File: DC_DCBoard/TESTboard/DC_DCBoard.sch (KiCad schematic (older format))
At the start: 26 parts, among them J1 TSV, J2 12V_OUT, J3 Conn_01x05, U1 DCM4623TD2J13D0T70, U2 LTV-817S, U3 TLP184, U4 LTV-817S

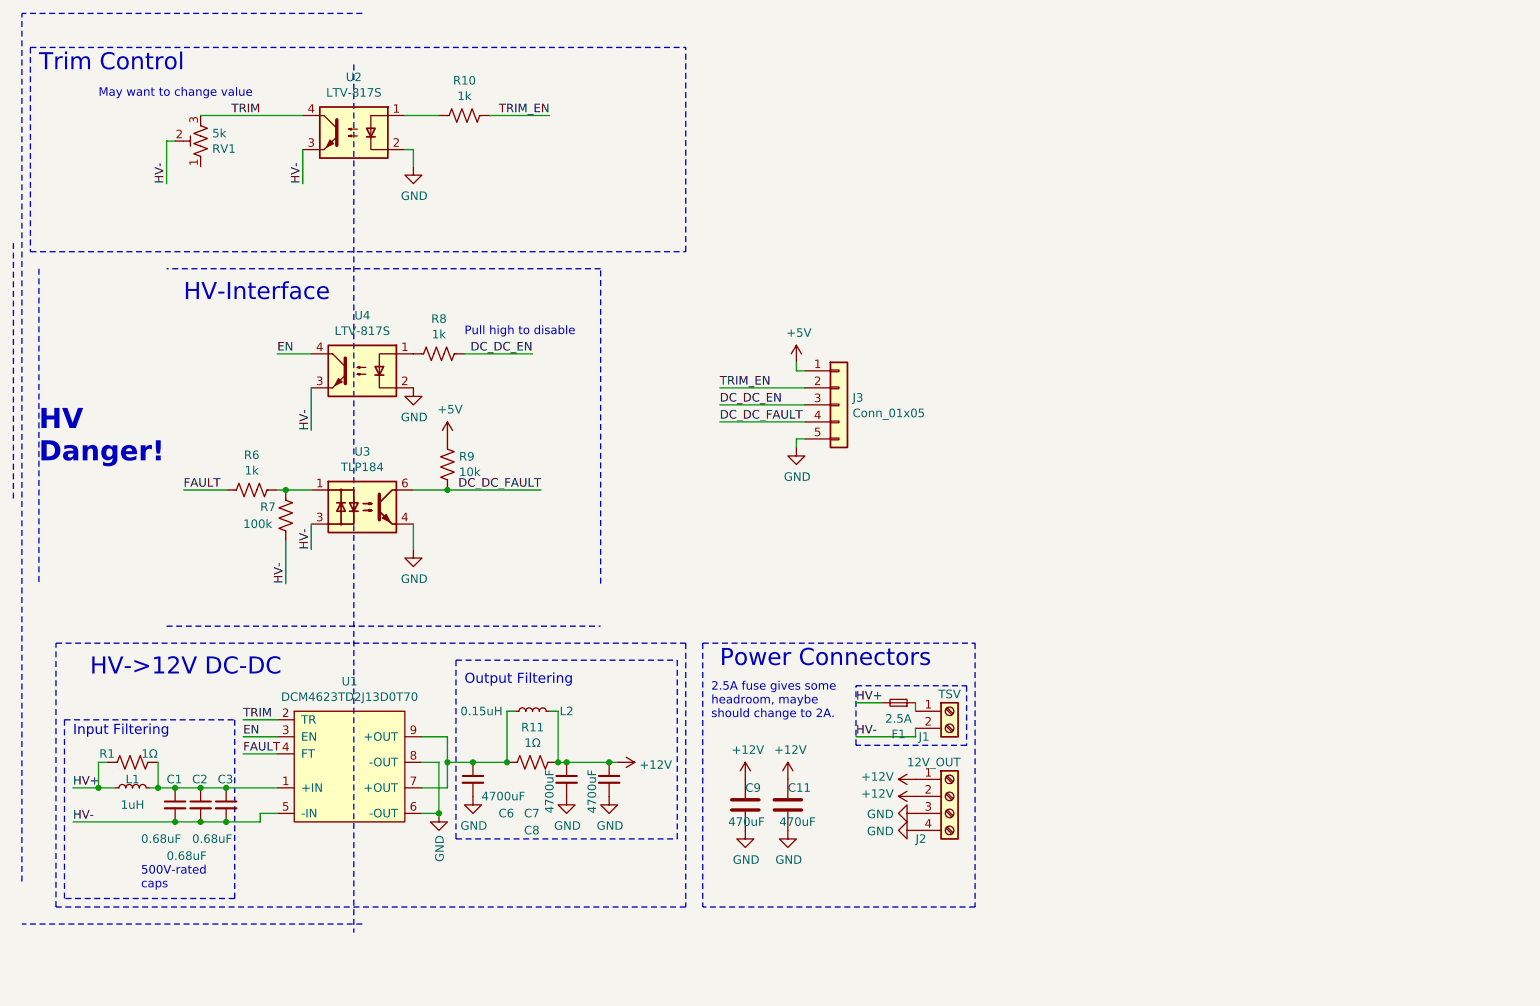
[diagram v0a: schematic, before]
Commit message: Made PDF schematic of DC/DC test board
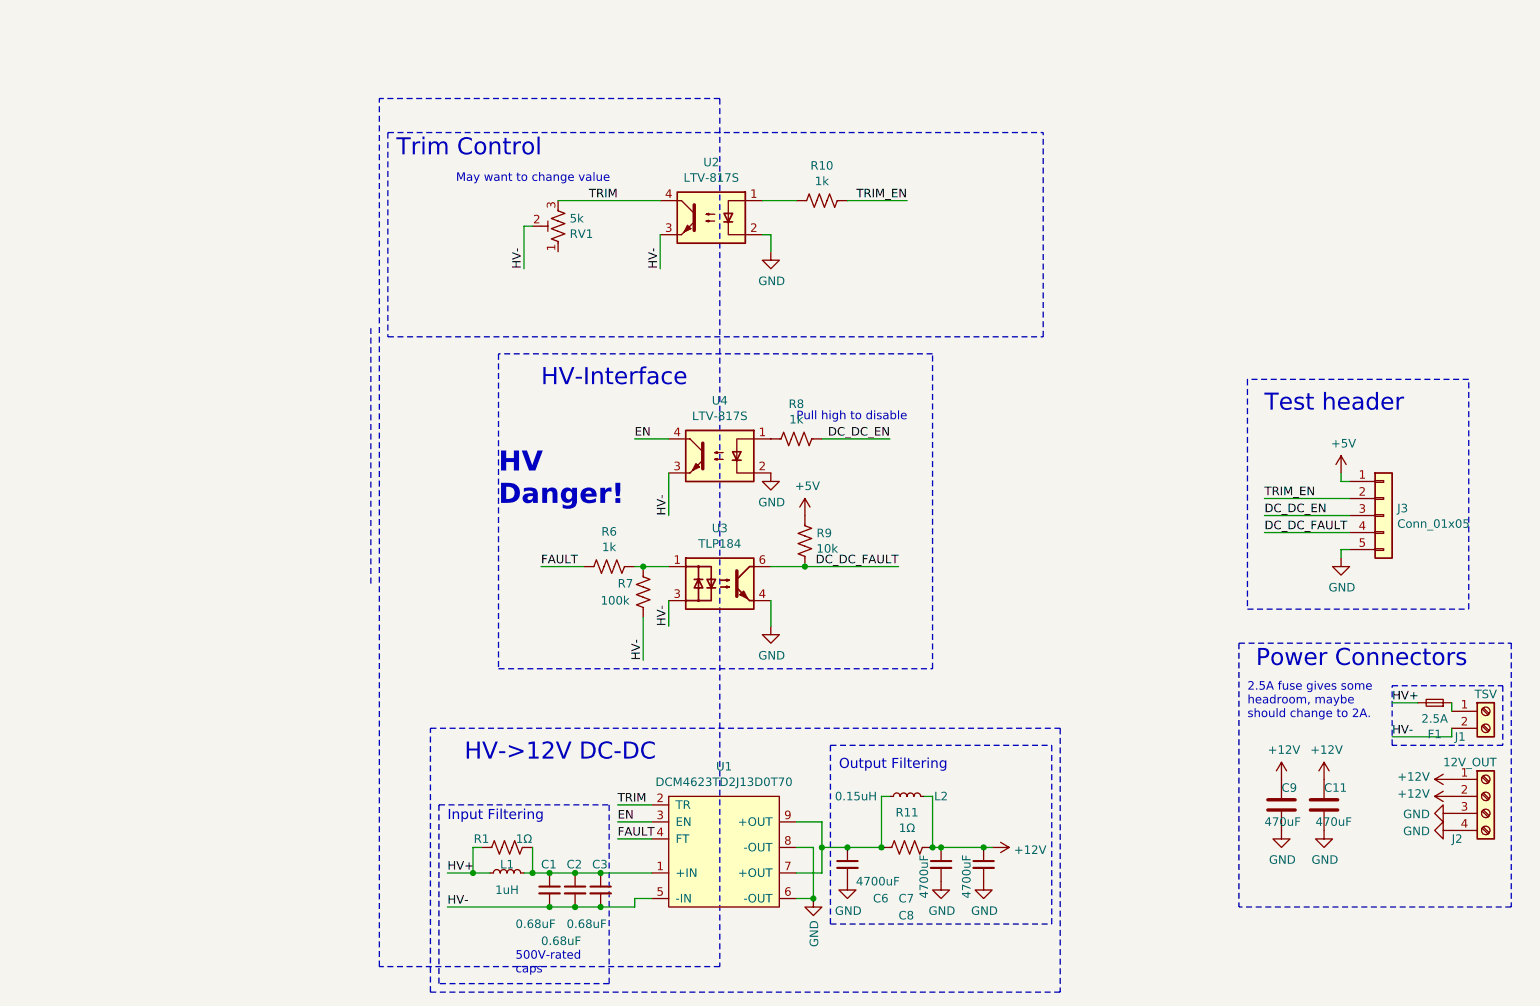
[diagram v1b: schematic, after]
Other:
- note added: "Test header"
- moved on the sheet: C1, C11, C2, C3, C6, C7, C8, C9, F1, J1, J2, J3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

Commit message: Fixed pot value on test board
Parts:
- added R2: 6.8k, Resistor_SMD:R_0603_1608Metric, symbol Device:R_US
- RV1: value 5k -> 50k; footprint Potentiometer_THT:Potentiometer_Piher_PT-15-V02_Vertical -> CustomFootprints:TC33X-503ECT-ND
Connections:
- net HV-: now also R2.2; no longer RV1.2
- new net: R2.1, RV1.2
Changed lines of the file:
@@
 P 3700 1800
 F 0 "RV1" H 3632 1846 50  0000 R CNN
-F 1 "5k" H 3632 1755 50  0000 R CNN
-F 2 "Potentiometer_THT:Potentiometer_Piher_PT-15-V02_Vertical" H 3700 1800 50  0001 C CNN
+F 1 "50k" H 3632 1755 50  0000 R CNN
+F 2 "CustomFootprints:TC33X-503ECT-ND" H 3700 1800 50  0001 C CNN
 F 3 "~" H 3700 1800 50  0001 C CNN
 	1    3700 1800
@@
 Wire Notes Line
 	2700 1250 6550 1250
-Text Label 3500 2050 1    50   ~ 0
+Text Label 3200 2050 1    50   ~ 0
 HV-
 Wire Wire Line
@@
 Wire Wire Line
 	3550 1800 3500 1800
-Wire Wire Line
-	3500 1800 3500 2050
 Text Notes 3150 4950 0    100  ~ 0
 HV->12V DC-DC
@@
 Text Notes 7850 2900 0    100  ~ 0
 Test header
+$Comp
+L Device:R_US R2
+U 1 1 5C5B2FDF
+P 3350 1800
+F 0 "R2" V 3145 1800 50  0000 C CNN
+F 1 "6.8k" V 3236 1800 50  0000 C CNN
+F 2 "Resistor_SMD:R_0603_1608Metric" V 3390 1790 50  0001 C CNN
+F 3 "~" H 3350 1800 50  0001 C CNN
+	1    3350 1800
+	0    1    1    0
+$EndComp
+Wire Wire Line
+	3200 1800 3200 2050
 $EndSCHEMATC

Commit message: Getting there with layout of big board...
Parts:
- removed R7: 100k, Resistor_SMD:R_0603_1608Metric, symbol Device:R_US
- U1: symbol AEROParts:DCM4623TD2J13D0T70 -> DC_DCBoard-rescue:DCM4623TD2J13D0T70-AEROParts
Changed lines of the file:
@@
 $EndDescr
 $Comp
-L AEROParts:DCM4623TD2J13D0T70 U1
+L DC_DCBoard-rescue:DCM4623TD2J13D0T70-AEROParts U1
 U 1 1 5BDD1F41
 P 4650 5500
@@
 Text Label 3050 5800 0    50   ~ 0
 HV-
-Text Label 4200 4350 1    50   ~ 0
-HV-
 $Comp
 L Device:R_US R6
@@
 $EndComp
 Wire Wire Line
-	4200 4100 4200 4350
-$Comp
-L Device:R_US R7
-U 1 1 5BDD6180
-P 4200 3950
-F 0 "R7" H 4050 4000 50  0000 L CNN
-F 1 "100k" H 3950 3900 50  0000 L CNN
-F 2 "Resistor_SMD:R_0603_1608Metric" V 4240 3940 50  0001 C CNN
-F 3 "~" H 4200 3950 50  0001 C CNN
-	1    4200 3950
-	1    0    0    -1
-$EndComp
-Wire Wire Line
 	3850 3800 3600 3800
 Text Label 3600 3800 0    50   ~ 0
 FAULT
-Wire Wire Line
-	4150 3800 4200 3800
-Connection ~ 4200 3800
-Wire Wire Line
-	4200 3800 4350 3800
 Wire Wire Line
 	4250 5200 4050 5200
@@
 Wire Wire Line
 	3200 1800 3200 2050
+Wire Wire Line
+	4150 3800 4350 3800
 $EndSCHEMATC

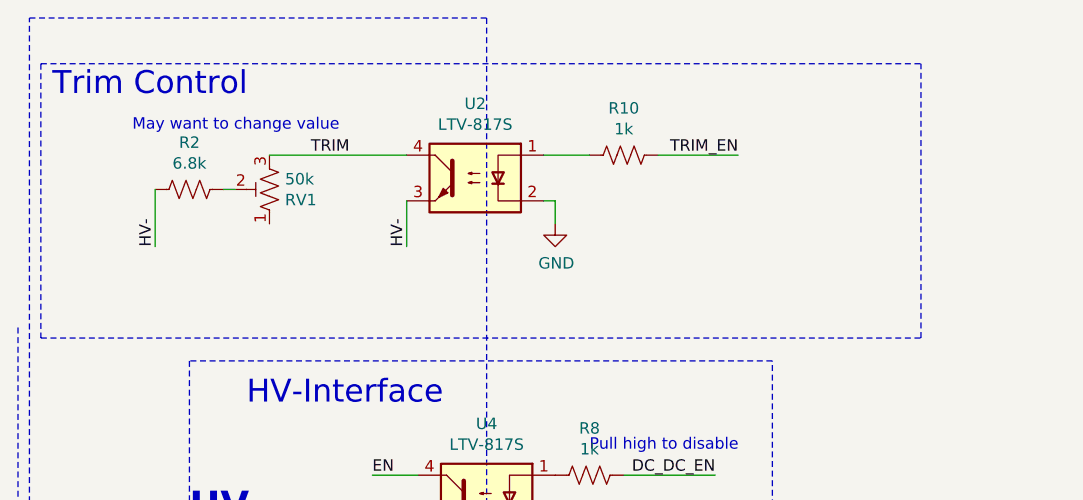
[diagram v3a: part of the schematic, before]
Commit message: Put Vicor on a removable module
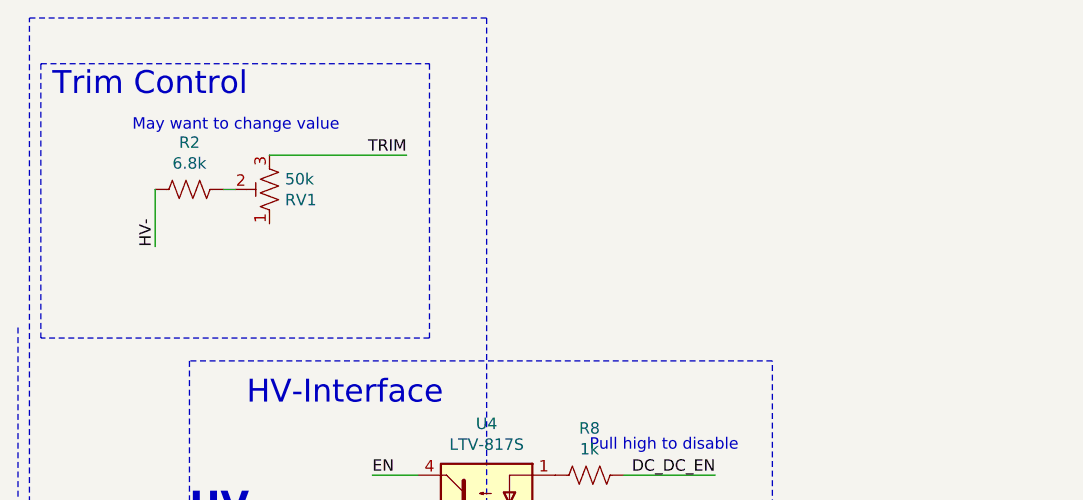
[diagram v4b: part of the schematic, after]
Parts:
- removed R10: 1k, Resistor_SMD:R_0603_1608Metric, symbol Device:R_US
- removed U2: LTV-817S, Package_DIP:SMDIP-4_W9.53mm, symbol Isolator:LTV-817S
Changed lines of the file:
@@
 Text Notes 7800 4400 0    100  ~ 0
 Power Connectors
-$Comp
-L Device:R_US R10
-U 1 1 5BEFADC1
-P 5250 1650
-F 0 "R10" V 5045 1650 50  0000 C CNN
-F 1 "1k" V 5136 1650 50  0000 C CNN
-F 2 "Resistor_SMD:R_0603_1608Metric" V 5290 1640 50  0001 C CNN
-F 3 "~" H 5250 1650 50  0001 C CNN
-	1    5250 1650
-	0    1    1    0
-$EndComp
-Wire Wire Line
-	5400 1650 5750 1650
-Text Label 5750 1650 2    50   ~ 0
-TRIM_EN
 Wire Notes Line
 	2700 1250 2700 2450
@@
 	-1   0    0    1
 $EndComp
-$Comp
-L power:GND #PWR012
-U 1 1 5BF48D46
-P 4950 1950
-F 0 "#PWR012" H 4950 1700 50  0001 C CNN
-F 1 "GND" H 4955 1777 50  0000 C CNN
-F 2 "" H 4950 1950 50  0001 C CNN
-F 3 "" H 4950 1950 50  0001 C CNN
-	1    4950 1950
-	1    0    0    -1
-$EndComp
-Wire Notes Line
-	2700 2450 6550 2450
-Wire Notes Line
-	6550 2450 6550 1250
-Wire Notes Line
-	2700 1250 6550 1250
 Text Label 3200 2050 1    50   ~ 0
 HV-
-Wire Wire Line
-	4900 1850 4950 1850
-Wire Wire Line
-	4950 1850 4950 1950
-Wire Wire Line
-	4900 1650 5100 1650
-Wire Wire Line
-	4300 1850 4300 2050
-Text Label 4300 2050 1    50   ~ 0
-HV-
-Text Label 4050 1650 2    50   ~ 0
+Text Label 4300 1650 2    50   ~ 0
 TRIM
-Wire Wire Line
-	3700 1650 4300 1650
 Wire Wire Line
 	3550 1800 3500 1800
@@
 $EndComp
 $Comp
-L Isolator:LTV-817S U2
-U 1 1 5C5B92F0
-P 4600 1750
-F 0 "U2" H 4600 2075 50  0000 C CNN
-F 1 "LTV-817S" H 4600 1984 50  0000 C CNN
-F 2 "Package_DIP:SMDIP-4_W9.53mm" H 4600 1450 50  0001 C CNN
-F 3 "http://www.us.liteon.com/downloads/LTV-817-827-847.PDF" H 4250 2050 50  0001 C CNN
-	1    4600 1750
-	-1   0    0    -1
-$EndComp
-$Comp
 L Isolator:LTV-817S U4
 U 1 1 5C5BC8D5
@@
 Wire Wire Line
 	4150 3800 4350 3800
+Wire Wire Line
+	3700 1650 4300 1650
+Wire Notes Line
+	2700 1250 4400 1250
+Wire Notes Line
+	4400 1250 4400 2450
+Wire Notes Line
+	4400 2450 2700 2450
 $EndSCHEMATC
